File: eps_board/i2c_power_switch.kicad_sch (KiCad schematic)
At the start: 6 parts, among them U25 MCP23008T-E/SS

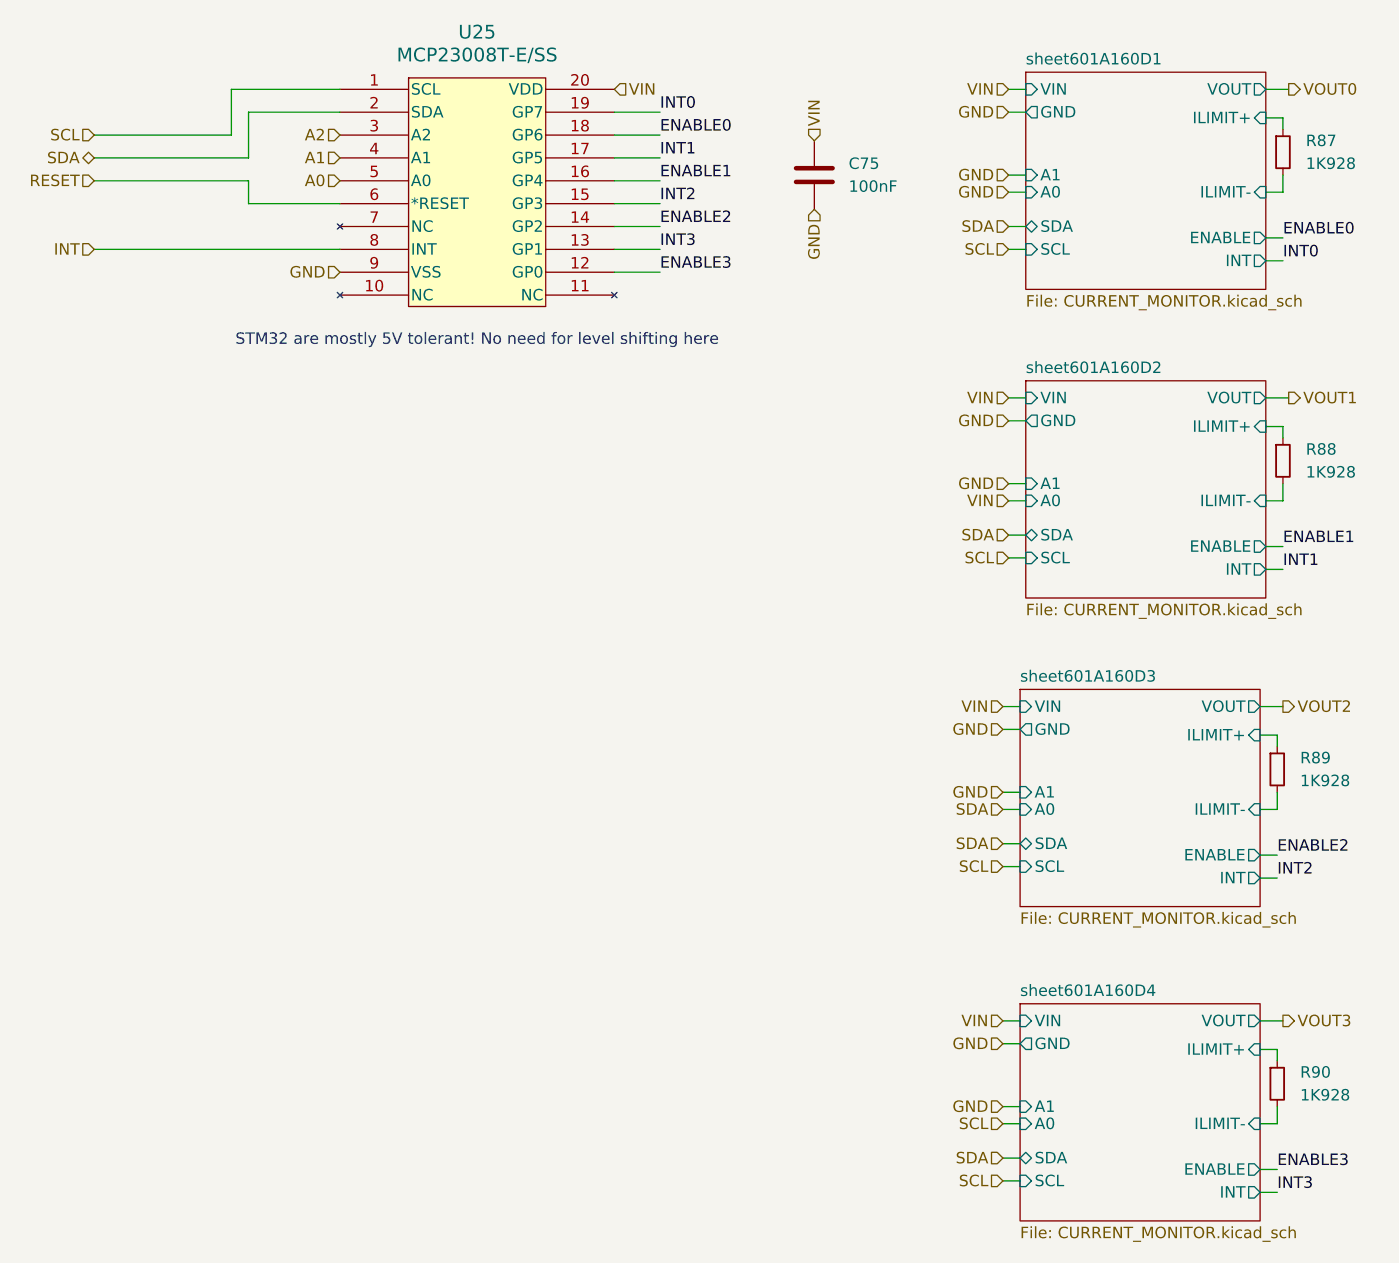
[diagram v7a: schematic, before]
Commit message: use small connectors in corners and on sides for sun sensors and solar cells
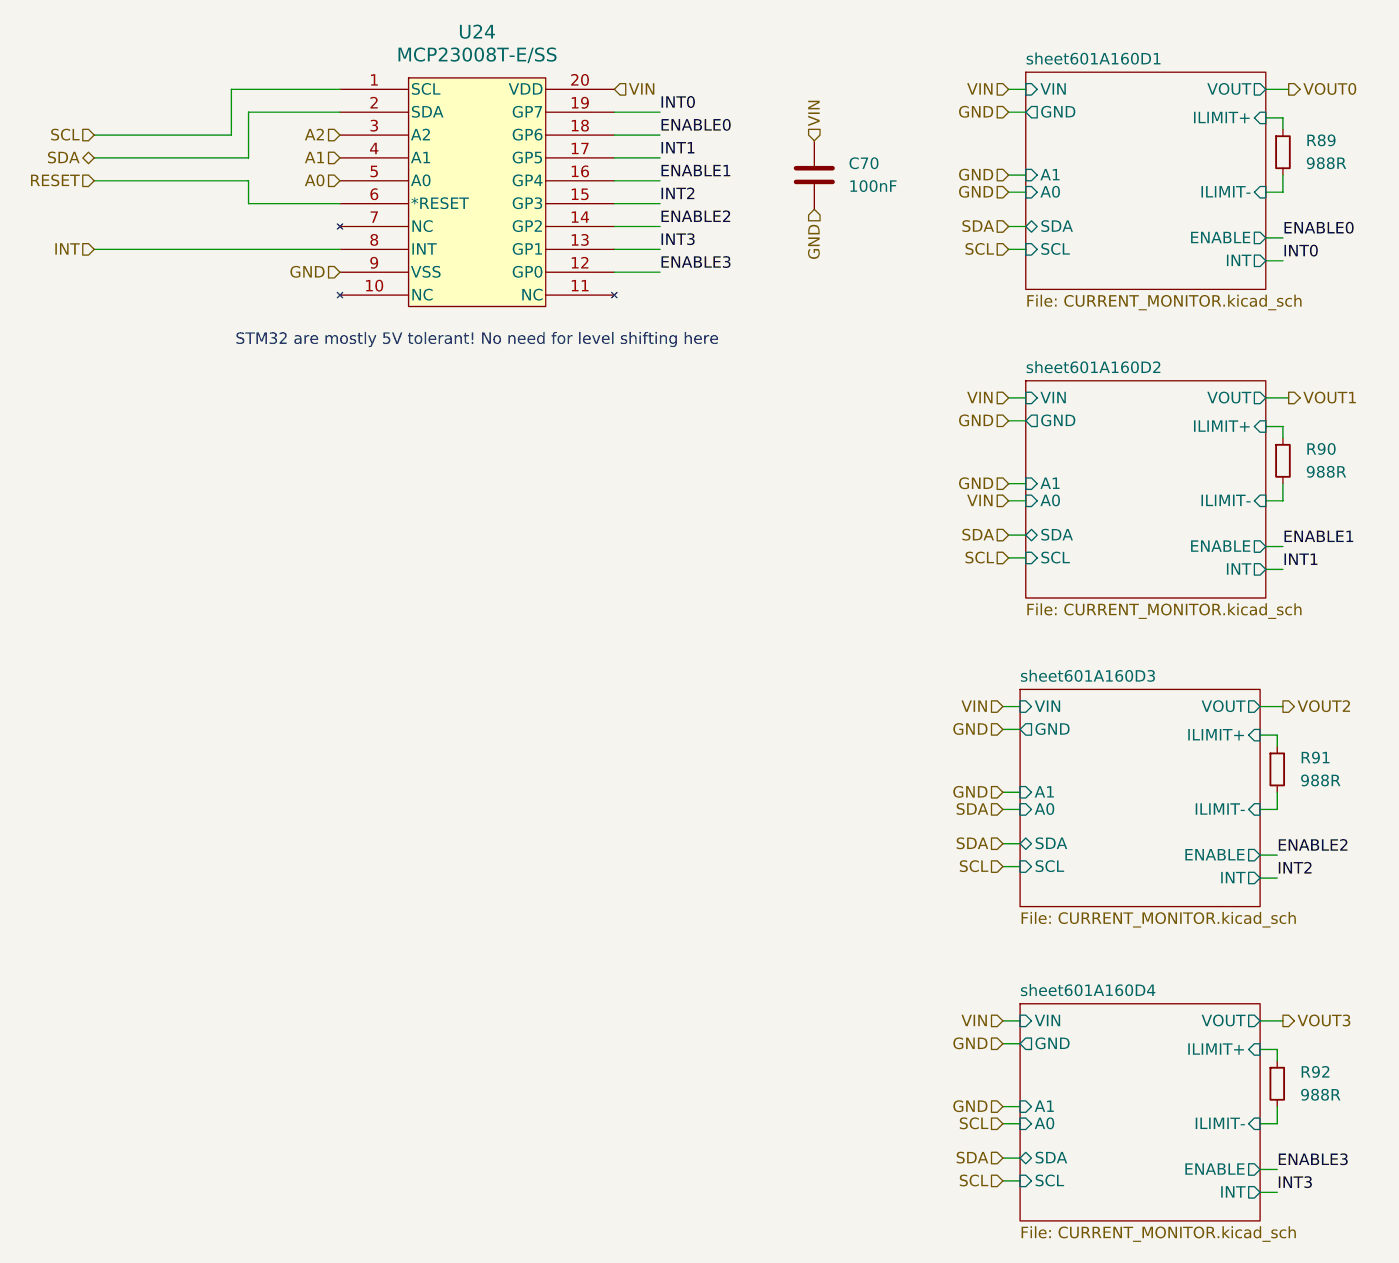
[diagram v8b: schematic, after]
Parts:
- R89: renamed from R87; value 1K928 -> 988R; Part Number RC0603FR-071K928L -> RT0603DRE07988RL; Tolerance 1 -> 0.5
- R90: renamed from R88; value 1K928 -> 988R; Part Number RC0603FR-071K928L -> RT0603DRE07988RL; Tolerance 1 -> 0.5
- R91: renamed from R89; value 1K928 -> 988R; Part Number RC0603FR-071K928L -> RT0603DRE07988RL; Tolerance 1 -> 0.5
- R92: renamed from R90; value 1K928 -> 988R; Part Number RC0603FR-071K928L -> RT0603DRE07988RL; Tolerance 1 -> 0.5
- renumbered C75 to C70, U25 to U24
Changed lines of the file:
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@@
 		(dnp no)
 		(fields_autoplaced yes)
-		(property "Reference" "C75"
+		(property "Reference" "C70"
 			(at 121.285 40.0049 0)
 			(effects
@@
 		)
 		(property "Tolerance" "10"
+			(at 117.475 41.275 0)
+			(effects
+				(font
+					(size 1.27 1.27)
+				)
+				(hide yes)
+			)
+		)
+		(property "Manufactorer" ""
 			(at 117.475 41.275 0)
 			(effects
@@
 			(project ""
 				(path "/05170af6-30ef-4c3a-b972-f098085da1bc/53211e67-c677-4be8-893d-9825fa308902"
-					(reference "C75")
+					(reference "C70")
 					(unit 1)
 				)
@@
 		(dnp no)
 		(fields_autoplaced yes)
-		(property "Reference" "R88"
+		(property "Reference" "R90"
 			(at 172.085 71.7549 0)
 			(effects
@@
 			)
 		)
-		(property "Value" "1K928"
+		(property "Value" "988R"
 			(at 172.085 74.2949 0)
 			(effects
@@
 			)
 		)
-		(property "Datasheet" "https://www.yageo.com/upload/media/product/products/datasheet/rchip/PYu-RC_Group_51_RoHS_L_12.pdf"
+		(property "Datasheet" "https://www.yageo.com/upload/media/product/app/datasheet/rchip/pyu-rt_1-to-0.01_rohs_l.pdf"
 			(at 169.545 73.025 0)
 			(effects
@@
 			)
 		)
-		(property "Part Number" "RC0603FR-071K928L"
+		(property "Part Number" "RT0603DRE07988RL"
 			(at 169.545 73.025 0)
 			(effects
@@
 			)
 		)
-		(property "Tolerance" "1"
+		(property "Tolerance" "0.5"
+			(at 169.545 73.025 0)
+			(effects
+				(font
+					(size 1.27 1.27)
+				)
+				(hide yes)
+			)
+		)
+		(property "Manufactorer" ""
 			(at 169.545 73.025 0)
 			(effects
@@
 			(project "EPS"
 				(path "/05170af6-30ef-4c3a-b972-f098085da1bc/53211e67-c677-4be8-893d-9825fa308902"
-					(reference "R88")
+					(reference "R90")
 					(unit 1)
 				)
@@
 		(dnp no)
 		(fields_autoplaced yes)
-		(property "Reference" "R90"
+		(property "Reference" "R92"
 			(at 171.45 140.9699 0)
 			(effects
@@
 			)
 		)
-		(property "Value" "1K928"
+		(property "Value" "988R"
 			(at 171.45 143.5099 0)
 			(effects
@@
 			)
 		)
-		(property "Datasheet" "https://www.yageo.com/upload/media/product/products/datasheet/rchip/PYu-RC_Group_51_RoHS_L_12.pdf"
+		(property "Datasheet" "https://www.yageo.com/upload/media/product/app/datasheet/rchip/pyu-rt_1-to-0.01_rohs_l.pdf"
 			(at 168.91 142.24 0)
 			(effects
@@
 			)
 		)
-		(property "Part Number" "RC0603FR-071K928L"
+		(property "Part Number" "RT0603DRE07988RL"
 			(at 168.91 142.24 0)
 			(effects
@@
 			)
 		)
-		(property "Tolerance" "1"
+		(property "Tolerance" "0.5"
+			(at 168.91 142.24 0)
+			(effects
+				(font
+					(size 1.27 1.27)
+				)
+				(hide yes)
+			)
+		)
+		(property "Manufactorer" ""
 			(at 168.91 142.24 0)
 			(effects
@@
 			(project "EPS"
 				(path "/05170af6-30ef-4c3a-b972-f098085da1bc/53211e67-c677-4be8-893d-9825fa308902"
-					(reference "R90")
+					(reference "R92")
 					(unit 1)
 				)
@@
 		(dnp no)
 		(fields_autoplaced yes)
-		(property "Reference" "R87"
+		(property "Reference" "R89"
 			(at 172.085 37.4649 0)
 			(effects
@@
 			)
 		)
-		(property "Value" "1K928"
+		(property "Value" "988R"
 			(at 172.085 40.0049 0)
 			(effects
@@
 			)
 		)
-		(property "Datasheet" "https://www.yageo.com/upload/media/product/products/datasheet/rchip/PYu-RC_Group_51_RoHS_L_12.pdf"
+		(property "Datasheet" "https://www.yageo.com/upload/media/product/app/datasheet/rchip/pyu-rt_1-to-0.01_rohs_l.pdf"
 			(at 169.545 38.735 0)
 			(effects
@@
 			)
 		)
-		(property "Part Number" "RC0603FR-071K928L"
+		(property "Part Number" "RT0603DRE07988RL"
 			(at 169.545 38.735 0)
 			(effects
@@
 			)
 		)
-		(property "Tolerance" "1"
+		(property "Tolerance" "0.5"
+			(at 169.545 38.735 0)
+			(effects
+				(font
+					(size 1.27 1.27)
+				)
+				(hide yes)
+			)
+		)
+		(property "Manufactorer" ""
 			(at 169.545 38.735 0)
 			(effects
@@
 			(project "EPS"
 				(path "/05170af6-30ef-4c3a-b972-f098085da1bc/53211e67-c677-4be8-893d-9825fa308902"
-					(reference "R87")
+					(reference "R89")
 					(unit 1)
 				)
@@
 		(dnp no)
 		(fields_autoplaced yes)
-		(property "Reference" "R89"
+		(property "Reference" "R91"
 			(at 171.45 106.0449 0)
 			(effects
@@
 			)
 		)
-		(property "Value" "1K928"
+		(property "Value" "988R"
 			(at 171.45 108.5849 0)
 			(effects
@@
 			)
 		)
-		(property "Datasheet" "https://www.yageo.com/upload/media/product/products/datasheet/rchip/PYu-RC_Group_51_RoHS_L_12.pdf"
+		(property "Datasheet" "https://www.yageo.com/upload/media/product/app/datasheet/rchip/pyu-rt_1-to-0.01_rohs_l.pdf"
 			(at 168.91 107.315 0)
 			(effects
@@
 			)
 		)
-		(property "Part Number" "RC0603FR-071K928L"
+		(property "Part Number" "RT0603DRE07988RL"
 			(at 168.91 107.315 0)
 			(effects
@@
 			)
 		)
-		(property "Tolerance" "1"
+		(property "Tolerance" "0.5"
+			(at 168.91 107.315 0)
+			(effects
+				(font
+					(size 1.27 1.27)
+				)
+				(hide yes)
+			)
+		)
+		(property "Manufactorer" ""
 			(at 168.91 107.315 0)
 			(effects
@@
 			(project "EPS"
 				(path "/05170af6-30ef-4c3a-b972-f098085da1bc/53211e67-c677-4be8-893d-9825fa308902"
-					(reference "R89")
+					(reference "R91")
 					(unit 1)
 				)
@@
 		(dnp no)
 		(fields_autoplaced yes)
-		(property "Reference" "U25"
+		(property "Reference" "U24"
 			(at 80.01 25.4 0)
 			(effects
@@
 		)
 		(property "Part Number" "MCP23008T-E/SS"
+			(at 57.15 31.75 0)
+			(effects
+				(font
+					(size 1.27 1.27)
+				)
+				(hide yes)
+			)
+		)
+		(property "Manufactorer" ""
 			(at 57.15 31.75 0)
 			(effects
@@
 			(project ""
 				(path "/05170af6-30ef-4c3a-b972-f098085da1bc/53211e67-c677-4be8-893d-9825fa308902"
-					(reference "U25")
+					(reference "U24")
 					(unit 1)
 				)
